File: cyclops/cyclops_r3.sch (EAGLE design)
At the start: 141 parts, among them Q1 BC817, Q2 IRF510, Q3 BC817, T0 0, T1 0, T2 0, T3 0, U1 MCP4921, U10 TLV2374, U11 THS4281, U12 MAX4564, U13 ZXTD, U14 ZXTD, U2 ADG3301, U3 MAX4564, U4 LT1931, U5 LT1764A, U6 337L, U7 TLV3701, U8 ADR03, U9 OP1177, X1 SLP3, X2 SLP3, X3 SLP3

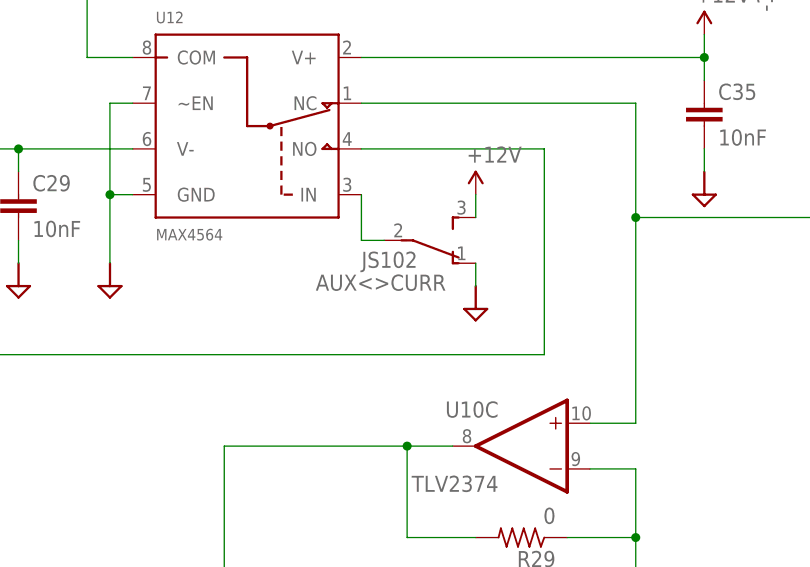
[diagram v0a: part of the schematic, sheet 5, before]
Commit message: First round of proofing revisions after building rev 3.5c board.
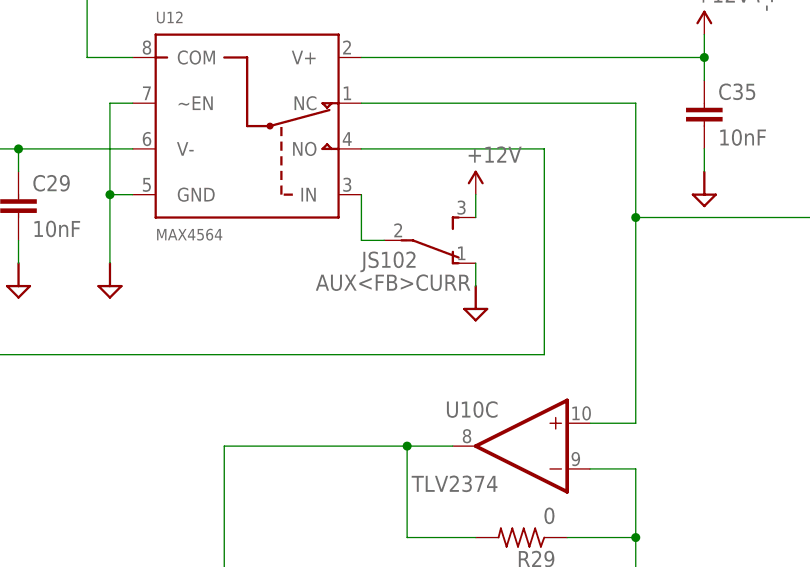
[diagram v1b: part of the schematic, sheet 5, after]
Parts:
- renumbered AUX<>CURR to AUX<FB>CURR
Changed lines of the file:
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@@
 <part name="C27" library="cyclops" deviceset="C" device="_0805" value="1uF"/>
 <part name="C25" library="cyclops" deviceset="C" device="_0603" value=".1uF"/>
-<part name="AUX&lt;&gt;CURR" library="cyclops" deviceset="SPDT" device="_JS" value="JS102"/>
+<part name="AUX&lt;FB&gt;CURR" library="cyclops" deviceset="SPDT" device="_JS" value="JS102"/>
 <part name="FRAME1" library="cyclops" deviceset="FRAME_A_L" device=""/>
 <part name="FRAME2" library="cyclops" deviceset="FRAME_A_L" device=""/>
@@
 <instance part="C27" gate="C" x="-17.78" y="20.32"/>
 <instance part="C25" gate="C" x="-25.4" y="20.32"/>
-<instance part="AUX&lt;&gt;CURR" gate="G$1" x="48.26" y="17.78" smashed="yes" rot="MR180">
+<instance part="AUX&lt;FB&gt;CURR" gate="G$1" x="48.26" y="17.78" smashed="yes" rot="MR180">
 <attribute name="NAME" x="38.1" y="13.97" size="1.778" layer="95" rot="MR180"/>
 <attribute name="VALUE" x="43.18" y="16.51" size="1.778" layer="96" rot="MR180"/>
@@
 </segment>
 <segment>
-<pinref part="AUX&lt;&gt;CURR" gate="G$1" pin="1"/>
+<pinref part="AUX&lt;FB&gt;CURR" gate="G$1" pin="1"/>
 <wire x1="55.88" y1="15.24" x2="55.88" y2="12.7" width="0.1524" layer="91"/>
 </segment>
@@
 </segment>
 <segment>
-<pinref part="AUX&lt;&gt;CURR" gate="G$1" pin="3"/>
+<pinref part="AUX&lt;FB&gt;CURR" gate="G$1" pin="3"/>
 <wire x1="55.88" y1="20.32" x2="55.88" y2="22.86" width="0.1524" layer="91"/>
 <pinref part="SUPPLY11" gate="G$1" pin="+12V"/>
@@
 <net name="IN" class="0">
 <segment>
-<pinref part="AUX&lt;&gt;CURR" gate="G$1" pin="2"/>
+<pinref part="AUX&lt;FB&gt;CURR" gate="G$1" pin="2"/>
 <wire x1="45.72" y1="17.78" x2="43.18" y2="17.78" width="0.1524" layer="91"/>
 <pinref part="U12" gate="G$1" pin="IN"/>

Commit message: Refactored library for rev. 3.5c.
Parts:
- R21: value 10k -> 220k
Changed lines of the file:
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@@
 <?xml version="1.0" encoding="utf-8"?>
 <!DOCTYPE eagle SYSTEM "eagle.dtd">
-<eagle version="6.5.0">
+<eagle version="7.5.0">
 <drawing>
 <settings>
@@
 <part name="U3" library="cyclops" deviceset="MAX4564" device=""/>
 <part name="SUPPLY12" library="cyclops" deviceset="+12V" device=""/>
-<part name="R21" library="cyclops" deviceset="R" device="_0603" value="10k"/>
+<part name="R21" library="cyclops" deviceset="R" device="_0603" value="220k"/>
 <part name="U$62" library="cyclops" deviceset="GND1" device=""/>
 <part name="Q3" library="cyclops" deviceset="BC817*" device="SMD" technology="-16" value="BC817"/>

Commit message: Final changes to board after rev 3.5c construction and testing.
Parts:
- R21: value 220k -> 110k
- R36: value 10k -> 2.2k
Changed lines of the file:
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@@
 <?xml version="1.0" encoding="utf-8"?>
 <!DOCTYPE eagle SYSTEM "eagle.dtd">
-<eagle version="7.5.0">
+<eagle version="6.5.0">
 <drawing>
 <settings>
@@
 <part name="U3" library="cyclops" deviceset="MAX4564" device=""/>
 <part name="SUPPLY12" library="cyclops" deviceset="+12V" device=""/>
-<part name="R21" library="cyclops" deviceset="R" device="_0603" value="220k"/>
+<part name="R21" library="cyclops" deviceset="R" device="_0603" value="110k"/>
 <part name="U$62" library="cyclops" deviceset="GND1" device=""/>
 <part name="Q3" library="cyclops" deviceset="BC817*" device="SMD" technology="-16" value="BC817"/>
-<part name="R36" library="cyclops" deviceset="R" device="_0603" value="10k"/>
+<part name="R36" library="cyclops" deviceset="R" device="_0603" value="2.2k"/>
 <part name="SUPPLY15" library="cyclops" deviceset="+12V" device=""/>
 <part name="CS3" library="cyclops" deviceset="R" device="_0603" value="0"/>
